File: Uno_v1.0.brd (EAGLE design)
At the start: 68.6 x 53.3 mm, 58 parts, among them CN1 POWER_JACK, CN2 47346-0001, IC1 AMS1117-5.0, IC2 AMS1117-3.3, IC3 MCP6002T-I/SN, J1 ICSP, J2 Digital2, J3 Digital1, J4 POWER, J5 Analog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

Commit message: Add some traces
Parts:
- C10, C11, C12, C13, C14, C15, C16, C18, C19, C4, C5, C6, C7, C8, C9: device rcl:C0603 -> rcl:C0402
- R1, R10, R11, R12, R2, R3, R4, R5, R6, R7, R8, R9: device rcl:R0603 -> rcl:R0402
- moved J4 17.8 mm to (45.7, 2.54), turned to 180 degrees
- moved R4 17.2 mm to (9.91, 32.4)
- moved C8 16.8 mm to (28.8, 42.2), turned to 180 degrees
- moved C7 16.2 mm to (28.8, 43.3), turned to 180 degrees
- moved R5 14.6 mm to (9.91, 31.0)
- moved J5 12.7 mm to (63.5, 2.54), turned to 180 degrees
- moved Q2 11.9 mm to (45.1, 39.1), turned to 0 degrees
- moved C13 9.62 mm to (43.1, 36.8), turned to 0 degrees
- moved C12 8.43 mm to (46.1, 36.8), turned to 180 degrees
- moved R6 6.74 mm to (45.2, 35.4), turned to 0 degrees
- moved C15 6.33 mm to (49.4, 35.4)
- moved C16 5.67 mm to (47.9, 23.1)
- moved C19 5.58 mm to (47.9, 21.7)
- moved C17 5.01 mm to (49.4, 38.6)
- moved C14 4.95 mm to (49.4, 36.8)
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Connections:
- new net USB_SHIELD: CN2.SH1, CN2.SH2, CN2.SH3, CN2.SH4, CN2.SH5, CN2.SH6
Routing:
- net 5V: track 0.00 -> 218.9 mm, vias 0 -> 11
- net RESET: track 0.00 -> 130.1 mm, vias 0 -> 3
- net A5_SCL: track 0.00 -> 96.7 mm, vias 0 -> 2
- net D0_RX: track 0.00 -> 96.7 mm, vias 0 -> 4
- net D1_TX: track 0.00 -> 95.5 mm, vias 0 -> 4
- net A4_SDA: track 0.00 -> 92.8 mm, vias 0 -> 2
- net D13_SCK: track 0.00 -> 78.0 mm, vias 0 -> 4
- net D11_MOSI: track 0.00 -> 77.2 mm, vias 0 -> 3
- net D12_MISO: track 0.00 -> 75.6 mm, vias 0 -> 3
- net VIN: track 0.00 -> 67.2 mm, vias 0 -> 1
- net 3.3V: track 0.00 -> 51.1 mm, vias 0 -> 2
- net AREF: track 0.00 -> 50.0 mm, vias 0 -> 1
- net D10_SS: track 0.00 -> 29.4 mm, vias 0 -> 1
- net GND: track 0.00 -> 29.4 mm, vias 0 -> 1
- net A3: track 0.00 -> 28.3 mm, vias 0 -> 1
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
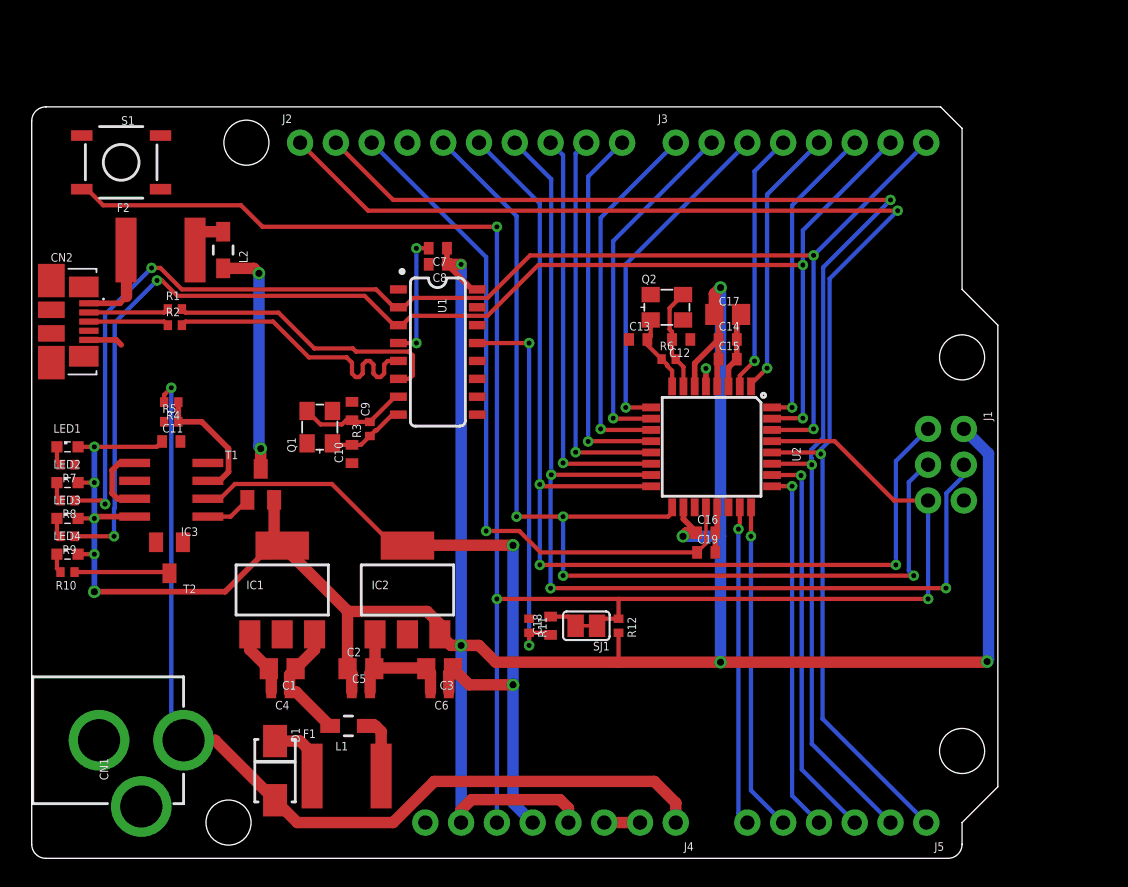
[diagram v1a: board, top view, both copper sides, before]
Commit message: Add some wires. Add top/bottom fills. Add top/bottom silks. Add pin descriptions.
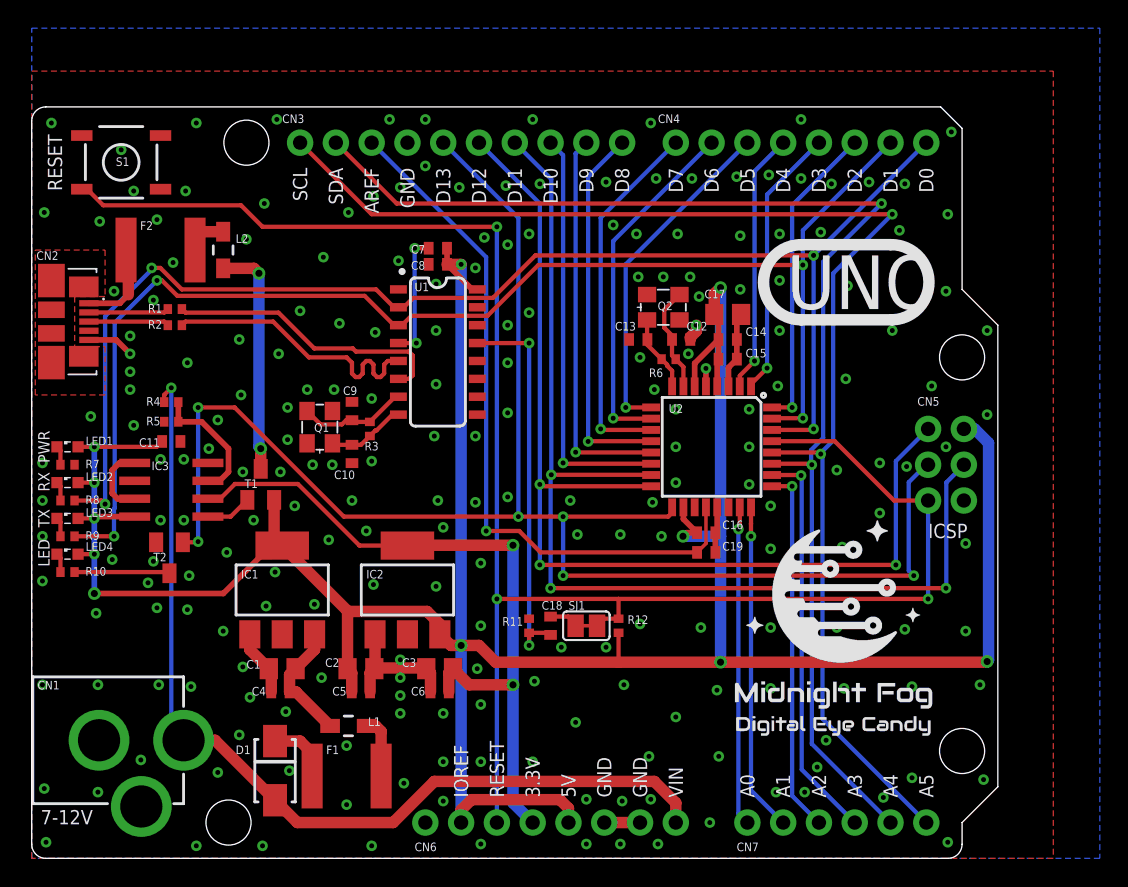
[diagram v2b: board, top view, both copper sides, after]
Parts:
- added LOGO1: MFDECLOGO_SQ_10MM, _my_logos:MFDEC_SQ_10MM
- added LOGO2: MFDECLOGO_L_40MM, _my_logos:MFDEC_L_40MM
- moved Q2 0.25 mm to (44.8, 39.1)
- renumbered J1 to CN5, J2 to CN3, J3 to CN4, J4 to CN6, J5 to CN7
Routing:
- net D13_SCK: track 78.0 -> 114.5 mm, vias 4 -> 6
- net GND: track 29.4 -> 31.5 mm, vias 1 -> 224
- net A4_SDA: track 92.8 -> 91.7 mm
- net A5_SCL: track 96.7 -> 96.0 mm
- added copper zone on layer 1, net GND
- added copper zone on layer 16, net GND
- added copper zone on layer 1, net USB_SHIELD
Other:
- board text added: "3.3V"
- board text added: "5V"
- board text added: "7-12V"
- board text added: "A0"
- board text added: "A1"
- board text added: "A2"
- board text added: "A3"
- board text added: "A4"
- board text added: "A5"
- board text added: "AREF"
- board text added: "D0"
- board text added: "D1"
- board text added: "D10"
- board text added: "D11"
- board text added: "D12"
- board text added: "D13"
- board text added: "D2"
- board text added: "D3"
- board text added: "D4"
- board text added: "D5"
- board text added: "D6"
- board text added: "D7"
- board text added: "D8"
- board text added: "D9"
- board text added: "GND"
- board text added: "ICSP"
- board text added: "IOREF"
- board text added: "LED"
- board text added: "PWR"
- board text added: "RESET"
- board text added: "RX"
- board text added: "SCL"
- board text added: "SDA"
- board text added: "TX"
- board text added: "UNO"
- board text added: "UNO v1 (c) Andriy Golovnya Designed in Germany http://redscorp.net"
- board text added: "VIN"

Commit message: Minor adjustments
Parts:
- CN3: value Digital2 -> DIGITAL10
- CN4: value Digital1 -> DIGITAL8
- CN6: value POWER -> POWER8
- CN7: value Analog -> ANALOG6
- T1: value PMOSFET -> AO3401A
- U2: value ATMEGA328P_TQFP -> ATMEGA328P-AU
- moved F2 0.38 mm to (9.14, 43.6)
- moved L2 0.38 mm to (13.6, 43.6)
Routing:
- net XUSB: track 6.29 -> 6.90 mm
- net VUSB: track 16.6 -> 17.2 mm
- net GND: vias 224 -> 227
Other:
- board text added: "+"
- board text added: "MISO"
- board text added: "MOSI"
- board text added: "PWM"
- board text added: "SCK"
- board text added: "SS"

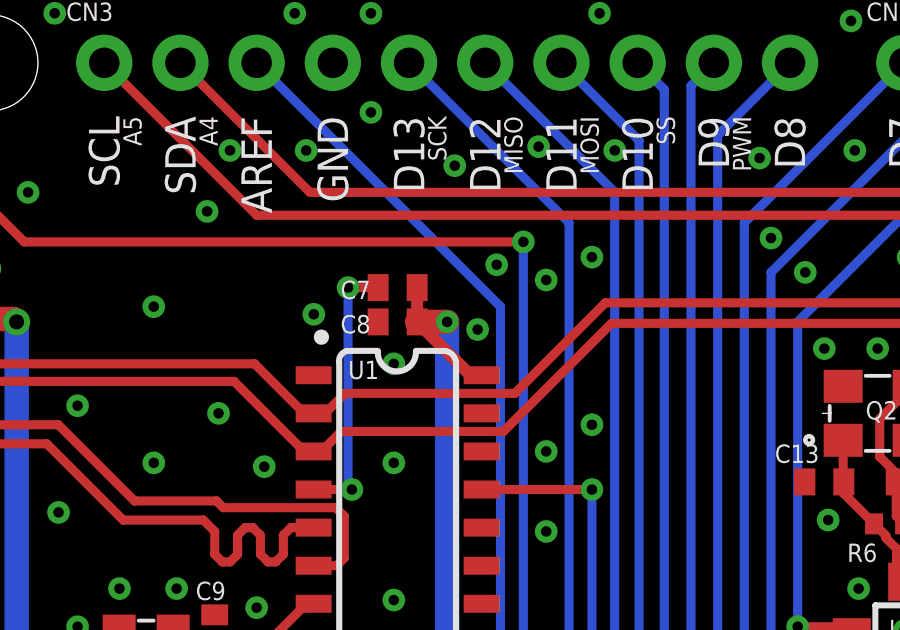
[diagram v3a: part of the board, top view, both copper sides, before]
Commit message: Fix connection of V3 pin of CH340G
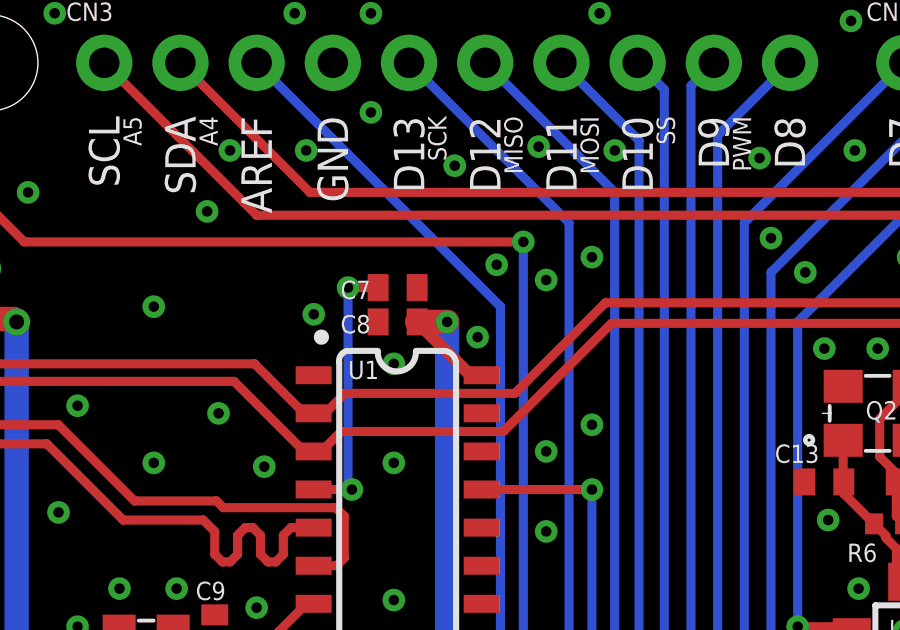
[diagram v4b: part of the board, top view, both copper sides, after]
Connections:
- net 5V: no longer C7.1
- net GND: now also C7.1
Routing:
- net 5V: track 219.4 -> 218.3 mm
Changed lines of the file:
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@@
 <drawing>
 <settings>
-<setting alwaysvectorfont="yes"/>
+<setting alwaysvectorfont="no"/>
 <setting verticaltext="up"/>
 </settings>
@@
 <via x="31.877" y="10.922" extent="1-16" drill="0.35"/>
 <via x="31.496" y="25.273" extent="1-16" drill="0.35"/>
-<via x="31.496" y="41.91" extent="1-16" drill="0.35"/>
+<via x="31.496" y="41.656" extent="1-16" drill="0.35"/>
 <via x="32.131" y="44.069" extent="1-16" drill="0.35"/>
 <via x="30.734" y="47.371" extent="1-16" drill="0.35"/>
@@
 <via x="14.986" y="39.497" extent="1-16" drill="0.35"/>
 <via x="22.86" y="39.116" extent="1-16" drill="0.35"/>
+<contactref element="C7" pad="1"/>
 </signal>
 <signal name="VIN" class="3">
@@
 <signal name="5V" class="3">
 <contactref element="U1" pad="16"/>
-<contactref element="C7" pad="1"/>
 <contactref element="C8" pad="1"/>
 <contactref element="IC3" pad="8"/>
@@
 <wire x1="48.753" y1="38.308" x2="48.453" y2="38.608" width="0.4064" layer="1"/>
 <wire x1="48.753" y1="36.83" x2="48.753" y2="35.433" width="0.4064" layer="1"/>
-<wire x1="29.479" y1="43.307" x2="29.479" y2="42.164" width="0.4064" layer="1"/>
 <wire x1="29.479" y1="42.164" x2="31.257" y2="40.386" width="0.4064" layer="1"/>
 <wire x1="31.257" y1="40.386" x2="31.629" y2="40.386" width="0.4064" layer="1"/>

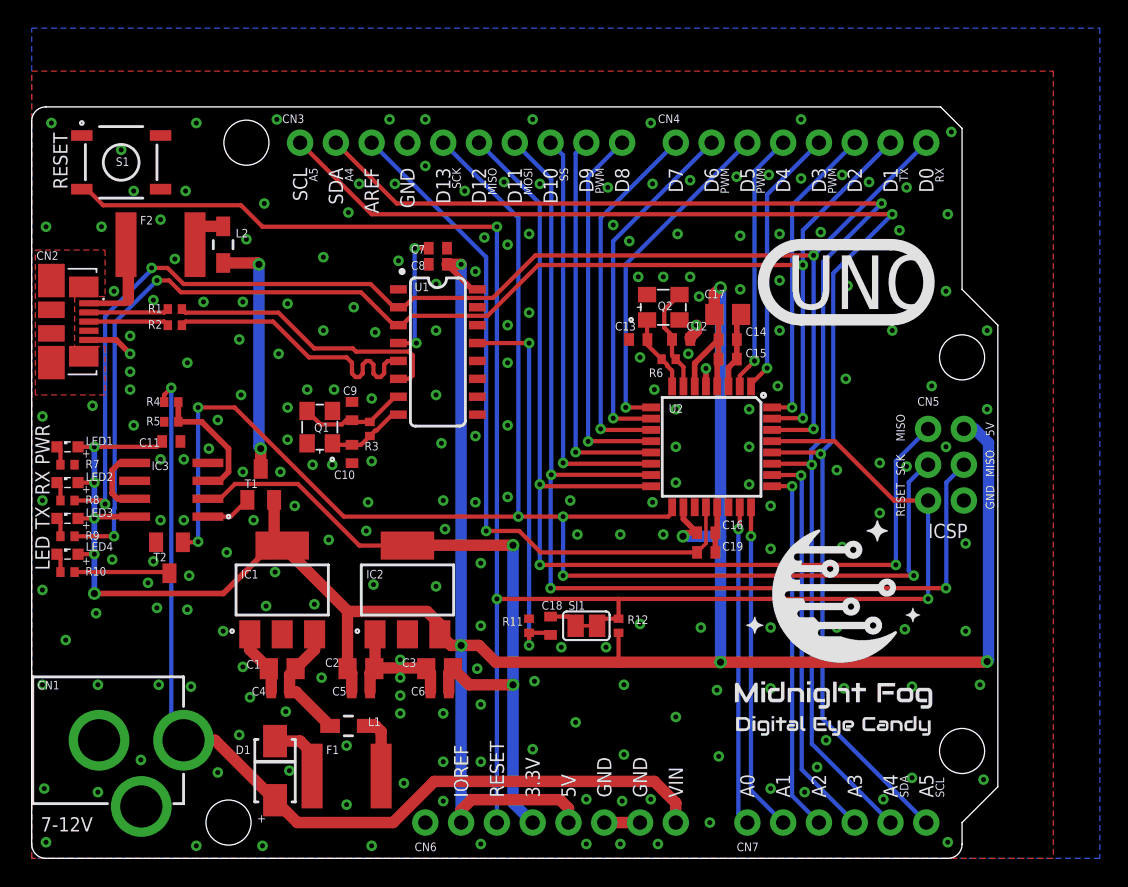
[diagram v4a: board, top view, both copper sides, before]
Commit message: Change capacitor sizes. Move stuff around.
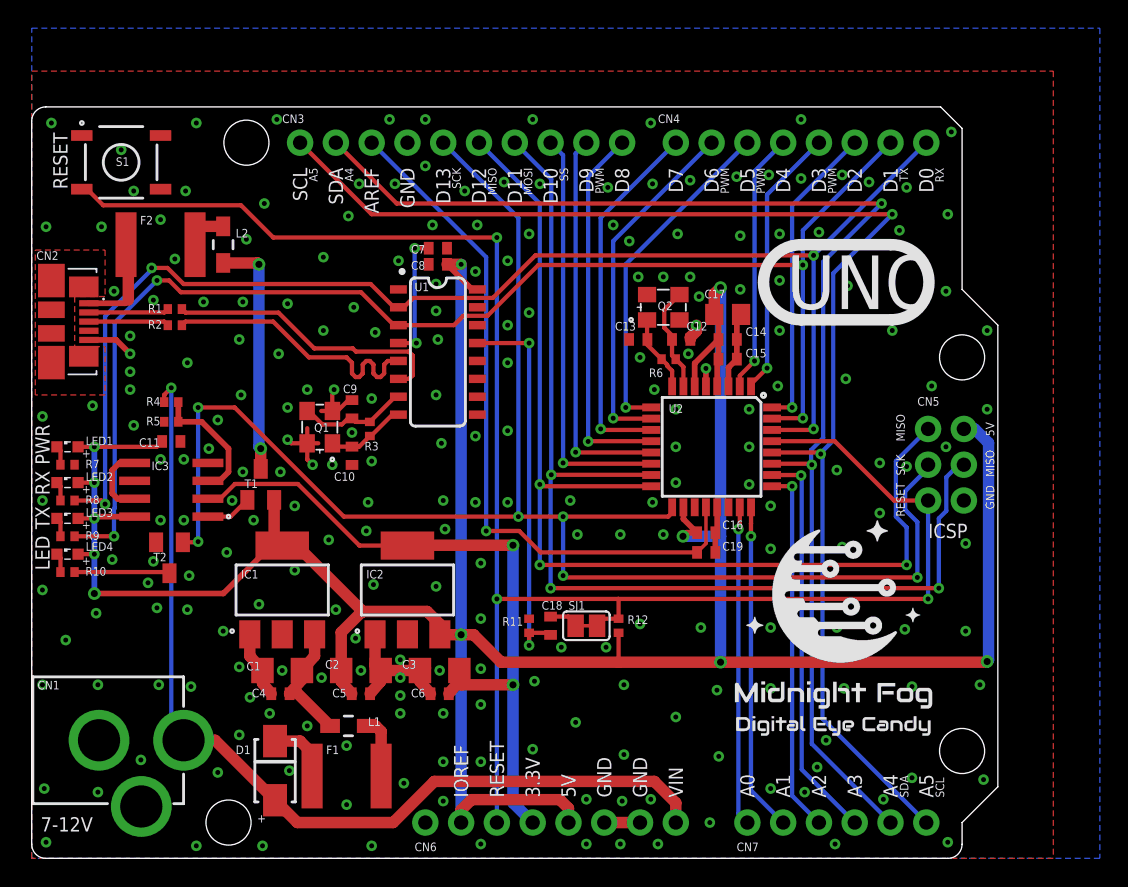
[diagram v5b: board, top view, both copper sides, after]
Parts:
- C1, C2, C3: device rcl:C0805 -> rcl:C1206
- moved LOGO2 7.47 mm to (78.9, -2.03)
- moved C10 0.13 mm to (22.7, 28.6)
- moved C4 0.13 mm to (17.7, 11.7)
- moved C5 0.13 mm to (23.4, 11.7)
- moved C6 0.13 mm to (29.0, 11.7)
- moved C1 0.13 mm to (17.8, 13.3)
- moved C2 0.13 mm to (23.4, 13.3)
- moved C3 0.13 mm to (29.0, 13.3)
- moved C9 0.13 mm to (22.7, 31.9)
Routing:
- net GND: track 31.5 -> 41.7 mm, vias 227 -> 237
- net D12_MISO: track 75.6 -> 76.7 mm
- net 5V: track 218.3 -> 219.2 mm
- net D13_SCK: track 114.5 -> 115.2 mm
- net 3.3V: track 51.4 -> 50.8 mm
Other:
- board text added: "Logic will get you from A to B. Imagination will take you everywhere. -- Albert Einstein"
- board text added: "UNO v1.0 (c) Andriy Golovnya Designed in Germany http://redscorp.net"
- board text removed: "UNO v1 (c) Andriy Golovnya Designed in Germany http://redscorp.net"

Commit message: Move stuff around. Change how SJ1 is closed by default. Add ground connections to Q2 and reset button.
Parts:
- moved L2 0.38 mm to (13.6, 43.9)
- moved F2 0.25 mm to (9.14, 43.8)
- moved C12 0.13 mm to (46.2, 36.8)
- moved C13 0.13 mm to (42.9, 36.8)
- turned SJ1 to 0 degrees
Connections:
- new net N$5: C18.2, SJ1.1
- net RESET: no longer C18.2, SJ1.1
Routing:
- net GND: track 41.7 -> 62.2 mm, vias 237 -> 239
- net RESET: track 129.6 -> 127.4 mm
- net N$5: track 0.00 -> 2.05 mm
